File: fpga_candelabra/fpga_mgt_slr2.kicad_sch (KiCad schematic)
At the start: 1 part, among them U1 XCVU13P-B2104

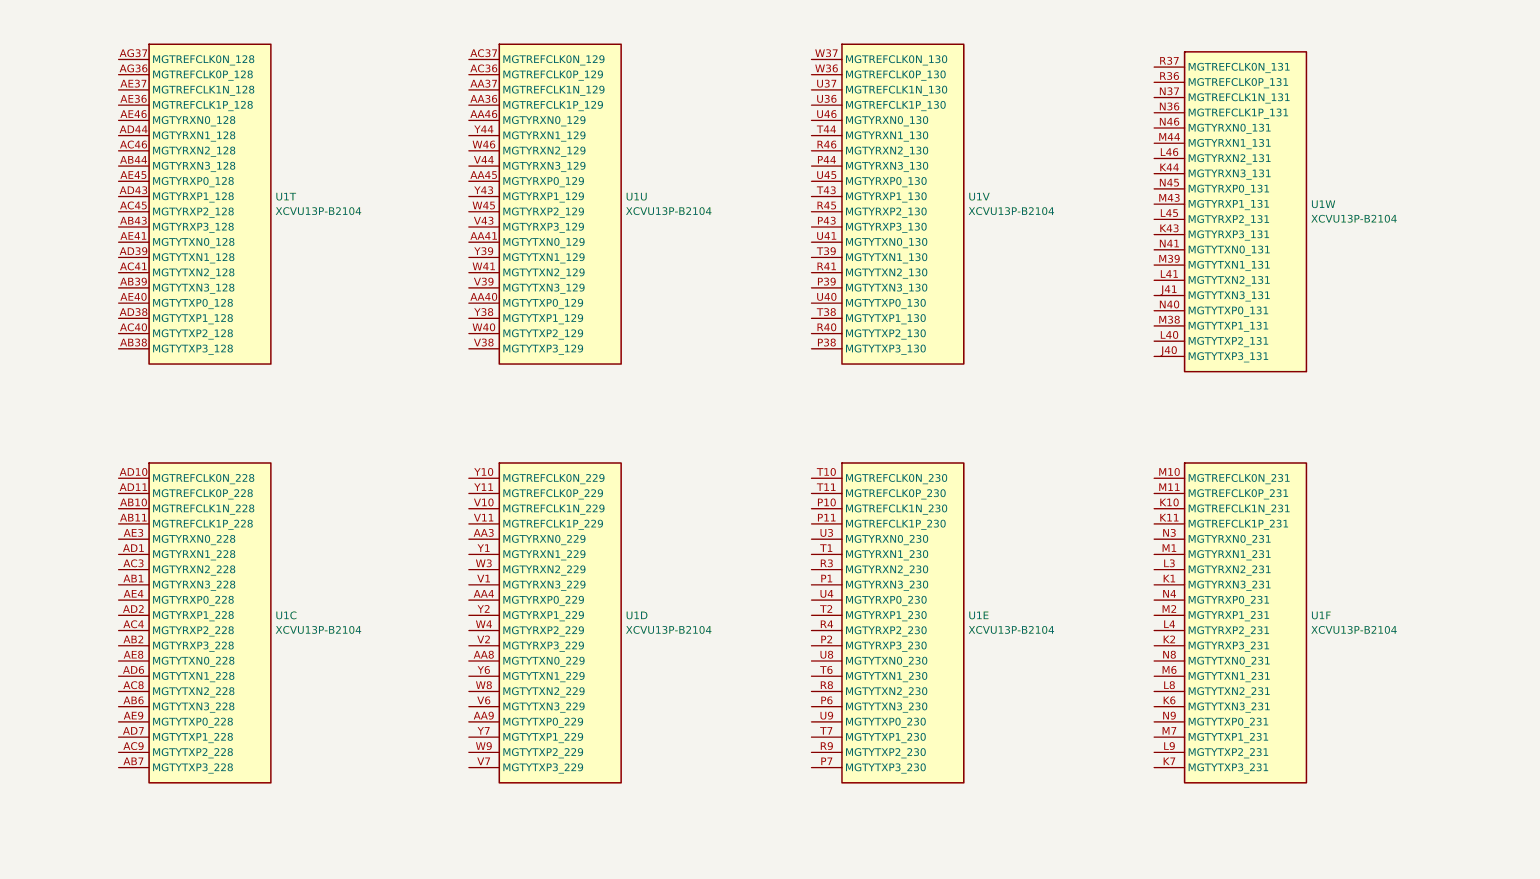
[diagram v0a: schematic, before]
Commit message: candelabra: add i-pex extension ports, remove FMC1
* update bank/mgt allocation
* add basic pcb floorplanning

Signed-off-by: Yichuan Gao <gaoyichuan000@gmail.com>
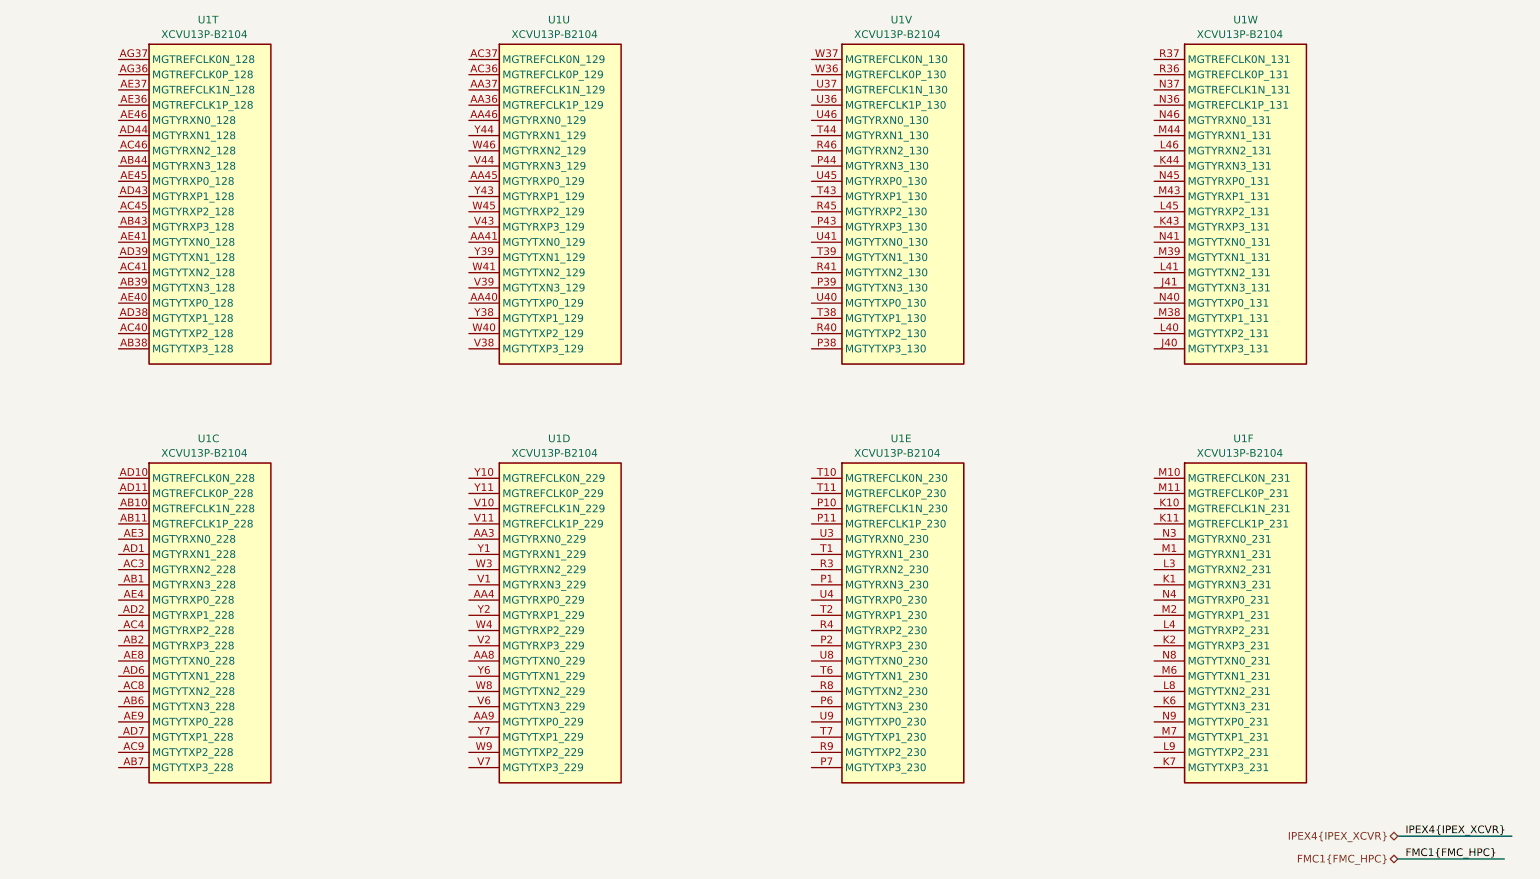
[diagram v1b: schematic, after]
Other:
- moved on the sheet: U1W
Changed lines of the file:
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@@
 	(generator_version "8.0")
 	(paper "A4")
+	(bus
+		(pts
+			(xy 264.16 158.75) (xy 283.21 158.75)
+		)
+		(stroke
+			(width 0)
+			(type default)
+		)
+	)
+	(bus
+		(pts
+			(xy 264.16 162.56) (xy 281.94 162.56)
+		)
+		(stroke
+			(width 0)
+			(type default)
+		)
+	)
+	(label "FMC1{FMC_HPC}"
+		(at 265.43 162.56 0)
+		(fields_autoplaced yes)
+		(effects
+			(font
+				(size 1.27 1.27)
+			)
+			(justify left bottom)
+		)
+	)
+	(label "IPEX4{IPEX_XCVR}"
+		(at 265.43 158.75 0)
+		(fields_autoplaced yes)
+		(effects
+			(font
+				(size 1.27 1.27)
+			)
+			(justify left bottom)
+		)
+	)
+	(hierarchical_label "IPEX4{IPEX_XCVR}"
+		(shape bidirectional)
+		(at 264.16 158.75 180)
+		(fields_autoplaced yes)
+		(effects
+			(font
+				(size 1.27 1.27)
+			)
+			(justify right)
+		)
+	)
+	(hierarchical_label "FMC1{FMC_HPC}"
+		(shape bidirectional)
+		(at 264.16 162.56 180)
+		(fields_autoplaced yes)
+		(effects
+			(font
+				(size 1.27 1.27)
+			)
+			(justify right)
+		)
+	)
 	(symbol
 		(lib_id "CHIPSAlliance_FPGA_Xilinx_Virtex_UltraScale_Plus:XCVU13P-B2104")
@@
 		(on_board yes)
 		(dnp no)
-		(fields_autoplaced yes)
 		(property "Reference" "U1"
-			(at 192.532 52.1278 0)
+			(at 179.578 22.606 0)
 			(effects
 				(font
@@
 		)
 		(property "Value" "XCVU13P-B2104"
-			(at 192.532 54.5521 0)
+			(at 173.482 25.0303 0)
 			(effects
 				(font
@@
 	(symbol
 		(lib_id "CHIPSAlliance_FPGA_Xilinx_Virtex_UltraScale_Plus:XCVU13P-B2104")
-		(at 223.52 30.48 0)
+		(at 223.52 29.21 0)
 		(unit 23)
 		(exclude_from_sim no)
@@
 		(on_board yes)
 		(dnp no)
-		(fields_autoplaced yes)
 		(property "Reference" "U1"
-			(at 249.682 53.3978 0)
+			(at 236.728 22.606 0)
 			(effects
 				(font
@@
 		)
 		(property "Value" "XCVU13P-B2104"
-			(at 249.682 55.8221 0)
+			(at 230.632 25.0303 0)
 			(effects
 				(font
@@
 		)
 		(property "Footprint" "CHIPSAlliance_Package_BGA:Xilinx_FHGB2104_VU13P_PkgLength"
-			(at 222.25 29.21 0)
+			(at 222.25 27.94 0)
 			(effects
 				(font
@@
 		)
 		(property "Datasheet" ""
-			(at 222.25 67.31 0)
+			(at 222.25 66.04 0)
 			(effects
 				(font
@@
 		)
 		(property "Description" "Virtex UltraScale+ 13P XCVU13P-B2104"
-			(at 223.52 30.48 0)
+			(at 223.52 29.21 0)
 			(effects
 				(font
@@
 		(on_board yes)
 		(dnp no)
-		(fields_autoplaced yes)
 		(property "Reference" "U1"
-			(at 249.682 121.9778 0)
+			(at 236.728 92.456 0)
 			(effects
 				(font
@@
 		)
 		(property "Value" "XCVU13P-B2104"
-			(at 249.682 124.4021 0)
+			(at 230.632 94.8803 0)
 			(effects
 				(font
@@
 		(on_board yes)
 		(dnp no)
-		(fields_autoplaced yes)
 		(property "Reference" "U1"
-			(at 135.382 121.9778 0)
+			(at 122.428 92.456 0)
 			(effects
 				(font
@@
 		)
 		(property "Value" "XCVU13P-B2104"
-			(at 135.382 124.4021 0)
+			(at 116.332 94.8803 0)
 			(effects
 				(font
@@
 		(on_board yes)
 		(dnp no)
-		(fields_autoplaced yes)
 		(property "Reference" "U1"
-			(at 76.962 52.1278 0)
+			(at 64.008 22.606 0)
 			(effects
 				(font
@@
 		)
 		(property "Value" "XCVU13P-B2104"
-			(at 76.962 54.5521 0)
+			(at 57.912 25.0303 0)
 			(effects
 				(font
@@
 		(on_board yes)
 		(dnp no)
-		(fields_autoplaced yes)
 		(property "Reference" "U1"
-			(at 135.382 52.1278 0)
+			(at 122.428 22.606 0)
 			(effects
 				(font
@@
 		)
 		(property "Value" "XCVU13P-B2104"
-			(at 135.382 54.5521 0)
+			(at 116.332 25.0303 0)
 			(effects
 				(font
@@
 		(on_board yes)
 		(dnp no)
-		(fields_autoplaced yes)
 		(property "Reference" "U1"
-			(at 76.962 121.9778 0)
+			(at 64.008 92.456 0)
 			(effects
 				(font
@@
 		)
 		(property "Value" "XCVU13P-B2104"
-			(at 76.962 124.4021 0)
+			(at 57.912 94.8803 0)
 			(effects
 				(font
@@
 		(on_board yes)
 		(dnp no)
-		(fields_autoplaced yes)
 		(property "Reference" "U1"
-			(at 192.532 121.9778 0)
+			(at 179.578 92.456 0)
 			(effects
 				(font
@@
 		)
 		(property "Value" "XCVU13P-B2104"
-			(at 192.532 124.4021 0)
+			(at 173.482 94.8803 0)
 			(effects
 				(font

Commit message: fpga_candelabra: major revision
* Finish DDR4 & QSFP+ & PCIe layout
* Change FMC to LPC
* Add mikroBUS extension
* 12V input & PDN updates
* FPGA config updates

Signed-off-by: Yichuan Gao <gaoyichuan000@gmail.com>
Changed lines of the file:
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@@
 	(generator_version "8.0")
 	(paper "A4")
-	(bus
-		(pts
-			(xy 264.16 158.75) (xy 283.21 158.75)
-		)
-		(stroke
-			(width 0)
-			(type default)
-		)
-	)
-	(bus
-		(pts
-			(xy 264.16 162.56) (xy 281.94 162.56)
-		)
-		(stroke
-			(width 0)
-			(type default)
-		)
-	)
-	(label "FMC1{FMC_HPC}"
-		(at 265.43 162.56 0)
-		(fields_autoplaced yes)
-		(effects
-			(font
-				(size 1.27 1.27)
-			)
-			(justify left bottom)
-		)
-	)
-	(label "IPEX4{IPEX_XCVR}"
-		(at 265.43 158.75 0)
-		(fields_autoplaced yes)
-		(effects
-			(font
-				(size 1.27 1.27)
-			)
-			(justify left bottom)
-		)
-	)
-	(hierarchical_label "IPEX4{IPEX_XCVR}"
-		(shape bidirectional)
-		(at 264.16 158.75 180)
-		(fields_autoplaced yes)
-		(effects
-			(font
-				(size 1.27 1.27)
-			)
-			(justify right)
-		)
-	)
-	(hierarchical_label "FMC1{FMC_HPC}"
-		(shape bidirectional)
-		(at 264.16 162.56 180)
-		(fields_autoplaced yes)
-		(effects
-			(font
-				(size 1.27 1.27)
-			)
-			(justify right)
-		)
-	)
 	(symbol
 		(lib_id "CHIPSAlliance_FPGA_Xilinx_Virtex_UltraScale_Plus:XCVU13P-B2104")

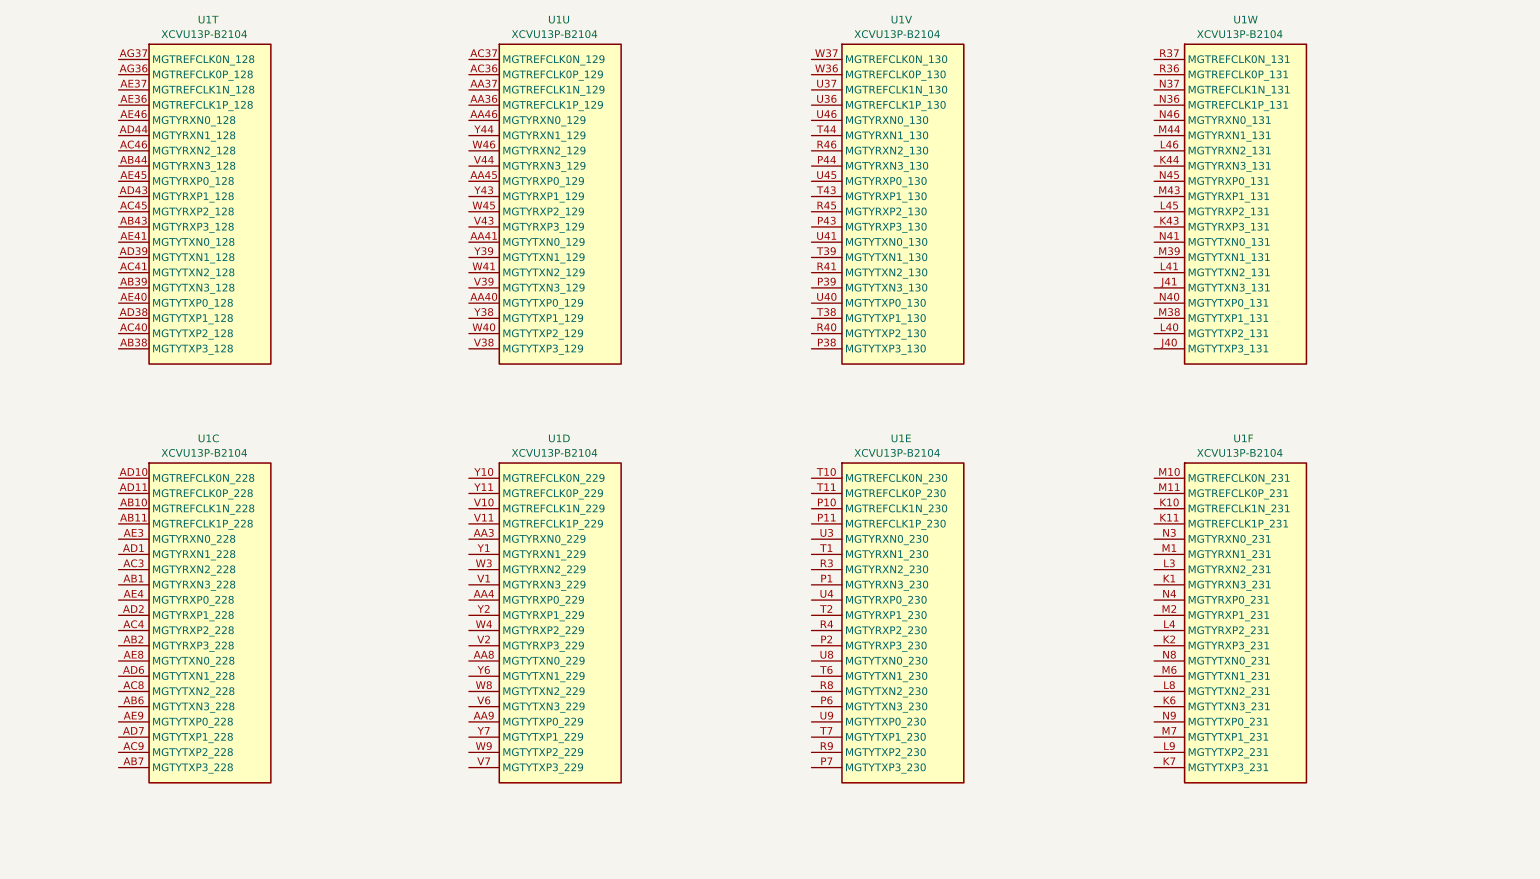
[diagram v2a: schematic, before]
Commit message: fpga_candelabra: sch & layout v0.5, pass basic ERC & DRC
Signed-off-by: Yichuan Gao <gaoyichuan000@gmail.com>
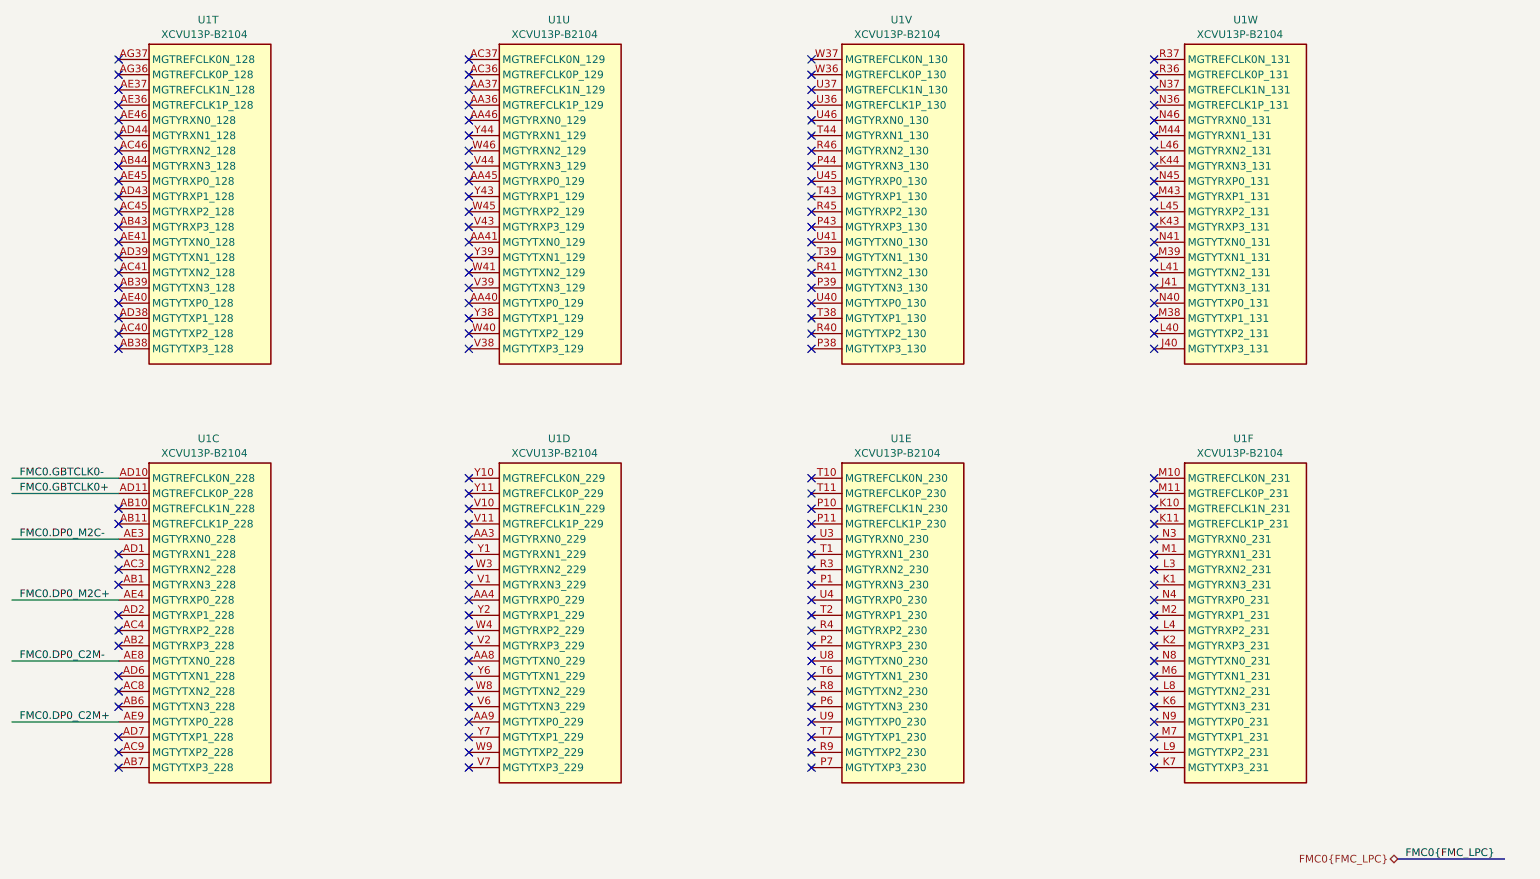
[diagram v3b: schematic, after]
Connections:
- net FMC0.GBTCLK0-: now reaches U1.AD10 (MGTREFCLK0N_228)
- net FMC0.GBTCLK0+: now reaches U1.AD11 (MGTREFCLK0P_228)
- net FMC0.DP0_M2C-: now reaches U1.AE3 (MGTYRXN0_228)
- net FMC0.DP0_M2C+: now reaches U1.AE4 (MGTYRXP0_228)
- net FMC0.DP0_C2M-: now reaches U1.AE8 (MGTYTXN0_228)
- net FMC0.DP0_C2M+: now reaches U1.AE9 (MGTYTXP0_228)
- no-connect marks 0 -> 154

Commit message: fpga_candelabra: add author & rev to schematics
Signed-off-by: Yichuan Gao <gaoyichuan000@gmail.com>
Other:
- company: (none) -> CHIPS Alliance
- title: (none) -> FPGA SLR2 MGT
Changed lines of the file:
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@@
 	(generator_version "8.0")
 	(paper "A4")
+	(title_block
+		(title "FPGA SLR2 MGT")
+		(date "2025-02-05")
+		(rev "0.2.0")
+		(company "CHIPS Alliance")
+		(comment 1 "Yichuan Gao")
+		(comment 2 "Yichuan Gao")
+	)
 	(no_connect
 		(at 166.37 127)

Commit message: fpga_candelabra: update to kicad 9.0
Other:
- company: CHIPS Alliance -> Sipeed
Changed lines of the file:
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@@
 (kicad_sch
-	(version 20231120)
+	(version 20250114)
 	(generator "eeschema")
-	(generator_version "8.0")
+	(generator_version "9.0")
 	(paper "A4")
 	(title_block
@@
 		(date "2025-02-05")
 		(rev "0.2.0")
-		(company "CHIPS Alliance")
-		(comment 1 "Yichuan Gao")
-		(comment 2 "Yichuan Gao")
+		(company "Sipeed")
+		(comment 1 "Sipeed")
+		(comment 2 "Sipeed")
 	)
 	(no_connect
